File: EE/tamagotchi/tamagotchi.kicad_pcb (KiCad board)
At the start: 4 copper layers, 34.8 x 38.8 mm, 46 parts, among them J1 Conn_01x02_Male, J3 Conn_01x07, J7 TAG_CONNECT, J8 Conn_01x02_Male, P1 USB_C_Plug_USB2.0, Q1 Q_NMOS_GSD, Q2 Q_NMOS_GSD, Q4 Q_NMOS_GSD, Q5 Q_PMOS_GSD, SW2 TL1260BQRBLK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

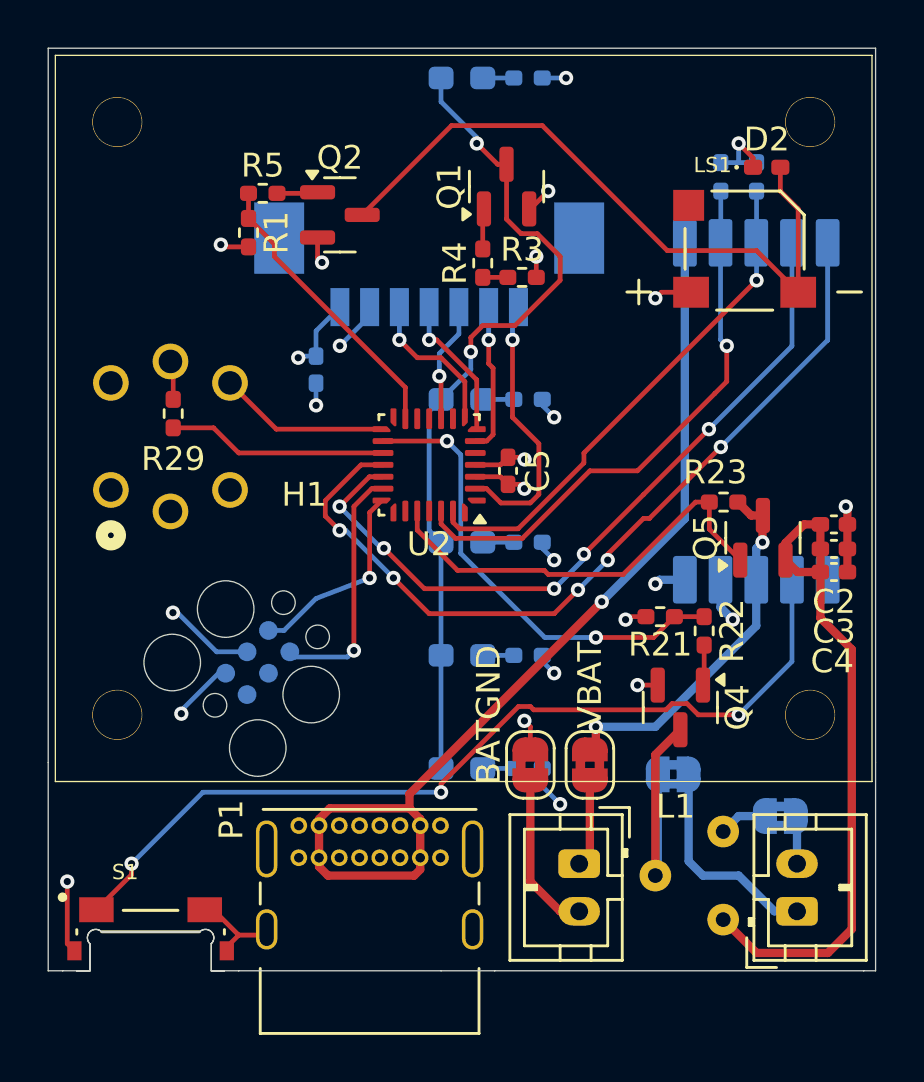
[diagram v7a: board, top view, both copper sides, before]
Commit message: Fixed board outline
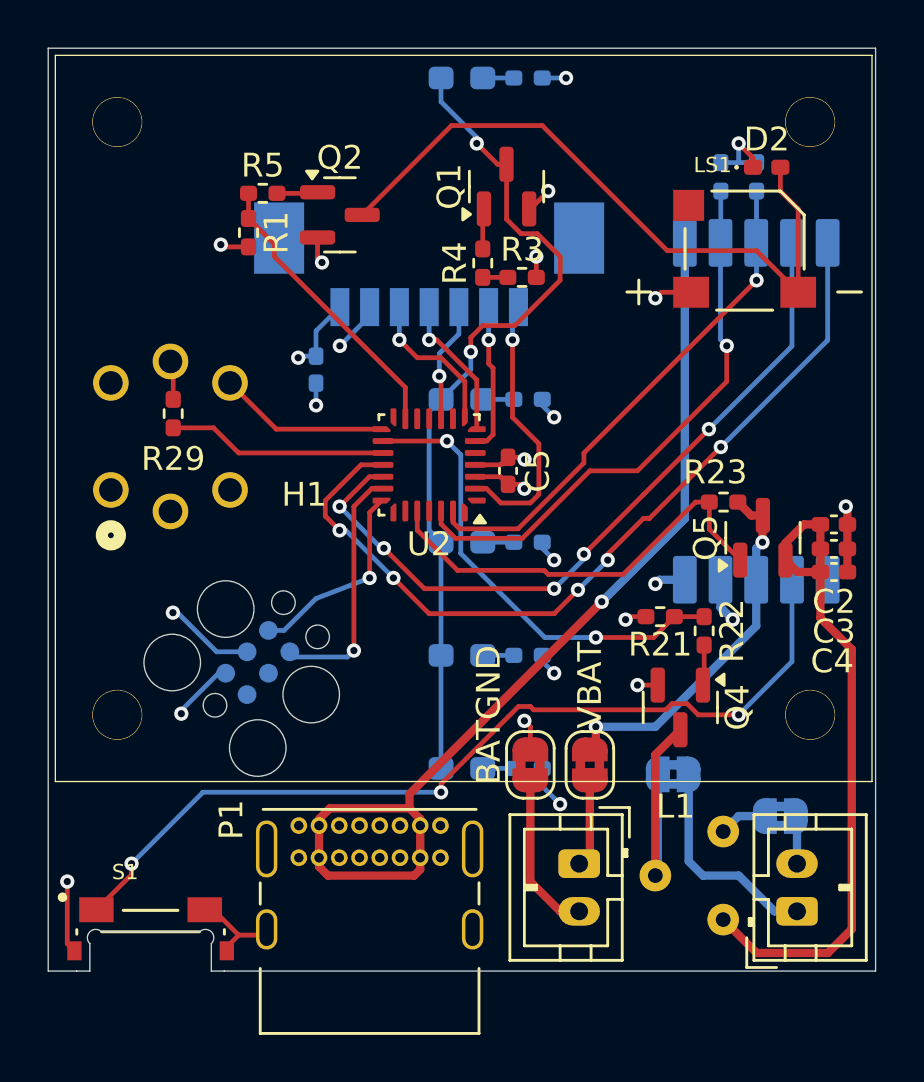
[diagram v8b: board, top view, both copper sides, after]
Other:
- outline, holes or cut-outs redrawn
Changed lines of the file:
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@@
 	)
 	(gr_line
-		(start 142.85 109.75)
-		(end 142.85 108.61)
+		(start 136 71)
+		(end 136 109.76)
 		(stroke
-			(width 0.05)
-			(type default)
-		)
-		(layer "Edge.Cuts")
-	)
-	(gr_arc
-		(start 137.75 108.61)
-		(mid 137.745 108.115)
-		(end 138.24 108.11)
-		(stroke
-			(width 0.05)
-			(type default)
+			(width 0.01)
+			(type solid)
 		)
 		(layer "Edge.Cuts")
 	)
 	(gr_line
-		(start 138.24 108.11)
-		(end 142.36 108.11)
+		(start 137.2 109.76)
+		(end 136 109.76)
 		(stroke
-			(width 0.05)
-			(type default)
-		)
-		(layer "Edge.Cuts")
-	)
-	(gr_line
-		(start 170.75 101)
-		(end 170.75 109.75)
-		(stroke
-			(width 0.05)
-			(type default)
-		)
-		(layer "Edge.Cuts")
-	)
-	(gr_line
-		(start 136 101)
-		(end 136 109.75)
-		(stroke
-			(width 0.05)
-			(type solid)
-		)
-		(layer "Edge.Cuts")
-	)
-	(gr_arc
-		(start 142.36 108.11)
-		(mid 142.855 108.115)
-		(end 142.85 108.61)
-		(stroke
-			(width 0.05)
-			(type default)
-		)
-		(layer "Edge.Cuts")
-	)
-	(gr_line
-		(start 152.5 109.75)
-		(end 144 109.75)
-		(stroke
-			(width 0.05)
-			(type default)
-		)
-		(layer "Edge.Cuts")
-	)
-	(gr_line
-		(start 152.5 109.75)
-		(end 154.75 109.75)
-		(stroke
-			(width 0.05)
-			(type default)
-		)
-		(layer "Edge.Cuts")
-	)
-	(gr_line
-		(start 137.2 109.75)
-		(end 136.61 109.75)
-		(stroke
-			(width 0.05)
+			(width 0.01)
 			(type solid)
 		)
@@
 		(end 170.75 71)
 		(stroke
-			(width 0.05)
-			(type default)
+			(width 0.01)
+			(type solid)
 		)
 		(layer "Edge.Cuts")
@@
 	(gr_line
 		(start 170.75 71)
-		(end 170.75 101)
+		(end 170.75 109.76)
 		(stroke
-			(width 0.05)
-			(type default)
-		)
-		(layer "Edge.Cuts")
-	)
-	(gr_line
-		(start 144 109.75)
-		(end 143.4 109.75)
-		(stroke
-			(width 0.05)
-			(type default)
-		)
-		(layer "Edge.Cuts")
-	)
-	(gr_line
-		(start 154.75 109.75)
-		(end 170.25 109.75)
-		(stroke
-			(width 0.05)
-			(type default)
-		)
-		(layer "Edge.Cuts")
-	)
-	(gr_line
-		(start 143.4 109.75)
-		(end 142.85 109.75)
-		(stroke
-			(width 0.05)
+			(width 0.01)
 			(type solid)
 		)
@@
 	)
 	(gr_line
-		(start 137.2 109.75)
-		(end 137.75 109.75)
+		(start 170.75 109.76)
+		(end 143.4 109.76)
 		(stroke
-			(width 0.05)
-			(type default)
-		)
-		(layer "Edge.Cuts")
-	)
-	(gr_line
-		(start 136 101)
-		(end 136 71)
-		(stroke
-			(width 0.05)
-			(type default)
-		)
-		(layer "Edge.Cuts")
-	)
-	(gr_line
-		(start 137.75 109.75)
-		(end 137.75 108.61)
-		(stroke
-			(width 0.05)
-			(type default)
-		)
-		(layer "Edge.Cuts")
-	)
-	(gr_line
-		(start 136 109.75)
-		(end 136.61 109.75)
-		(stroke
-			(width 0.05)
+			(width 0.01)
 			(type solid)
 		)
 		(layer "Edge.Cuts")
-	)
-	(gr_line
-		(start 170.75 109.75)
-		(end 170.25 109.75)
-		(stroke
-			(width 0.05)
-			(type default)
-		)
-		(layer "Edge.Cuts")
